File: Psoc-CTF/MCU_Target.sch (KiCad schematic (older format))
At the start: 69 parts, among them IC1 CY8C4248LQI-BL583, J4 Conn_01x04, J5 USB3076-XX-X_REVC, J6 Header 9x2, J7 Header 9x2, P1 Power, P2 Analog, P3 Digital, P4 Digital, P5 CONN_01X01, P6 CONN_01X01, P7 CONN_01X01, P8 CONN_01X01, U4 FM24C04B-GTR, U5 CY7C65211-24LTXI, Y1 24MHz, Y2 32.768Khz

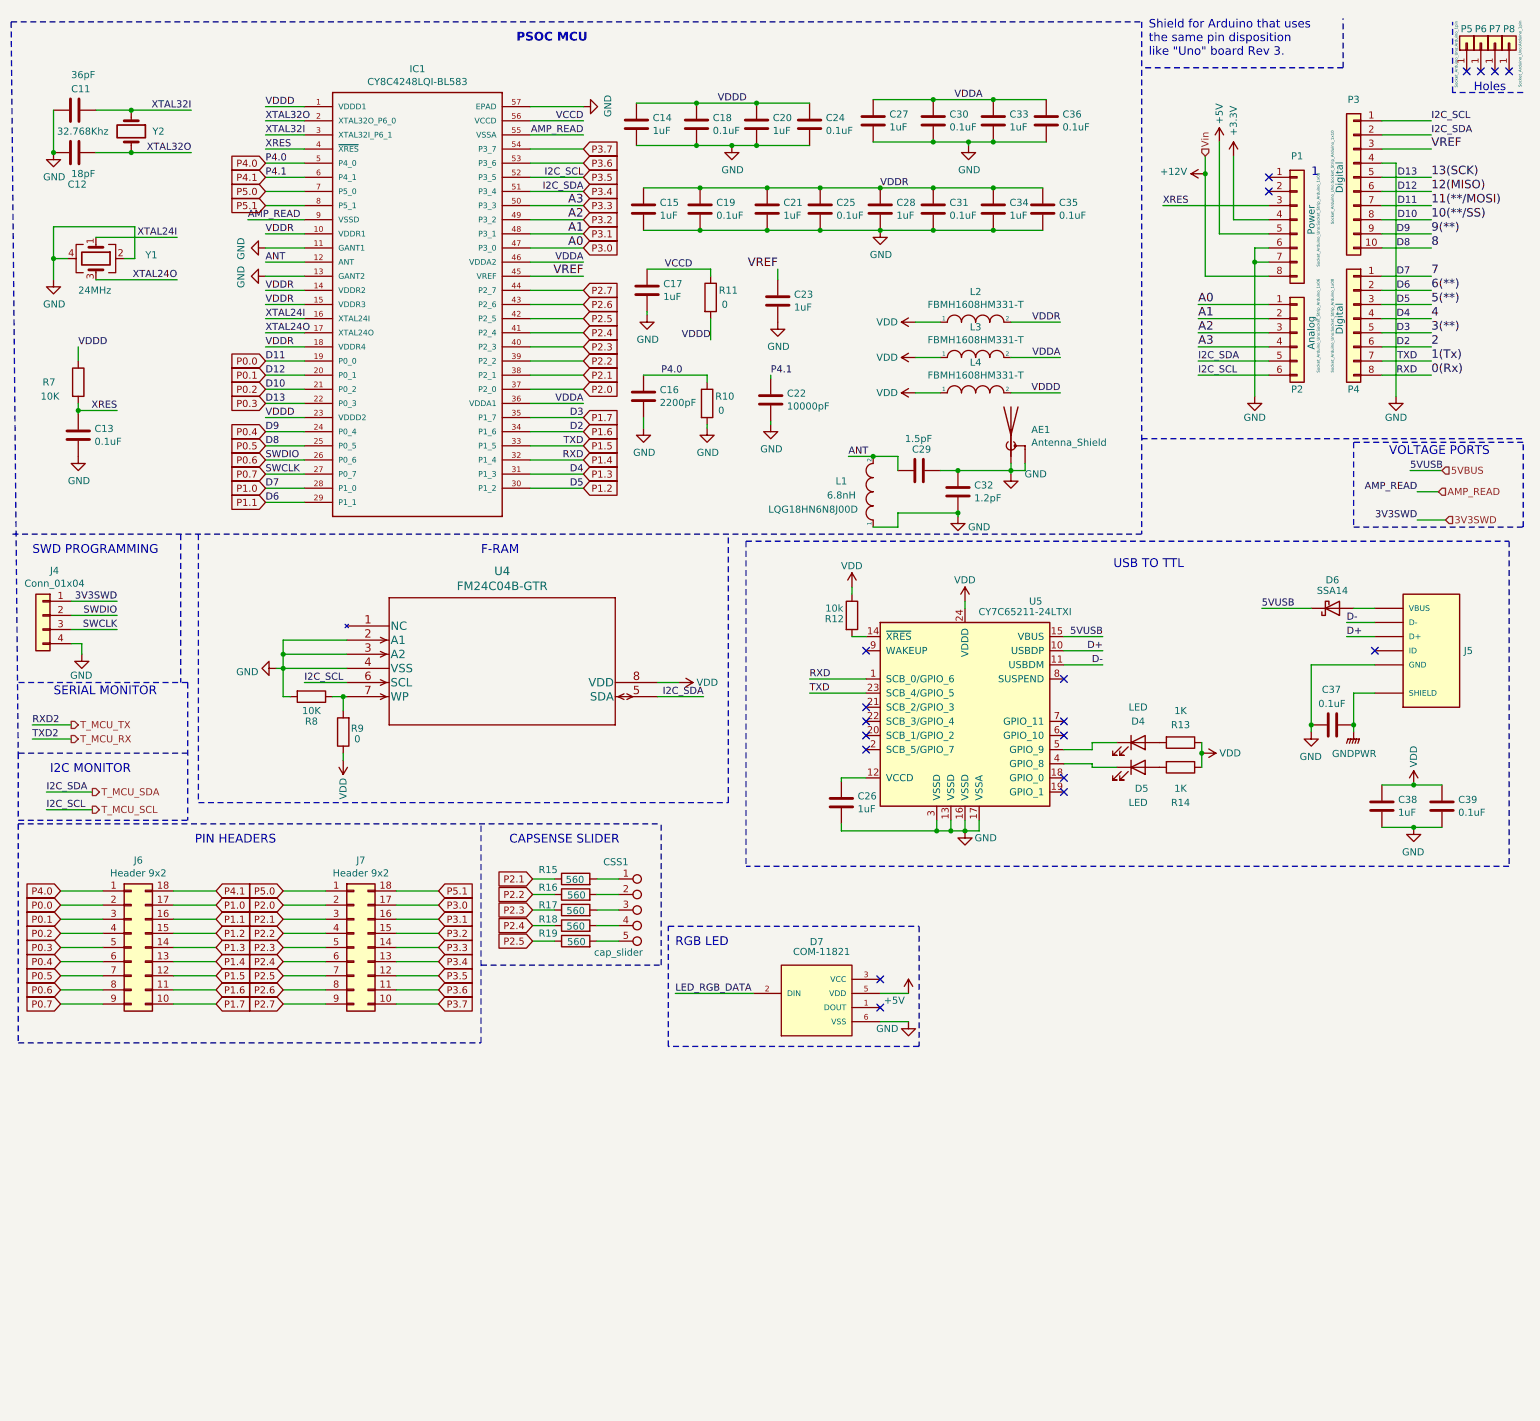
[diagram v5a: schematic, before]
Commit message: Anexo de nuevos pulsadores y arreglo de resistencias
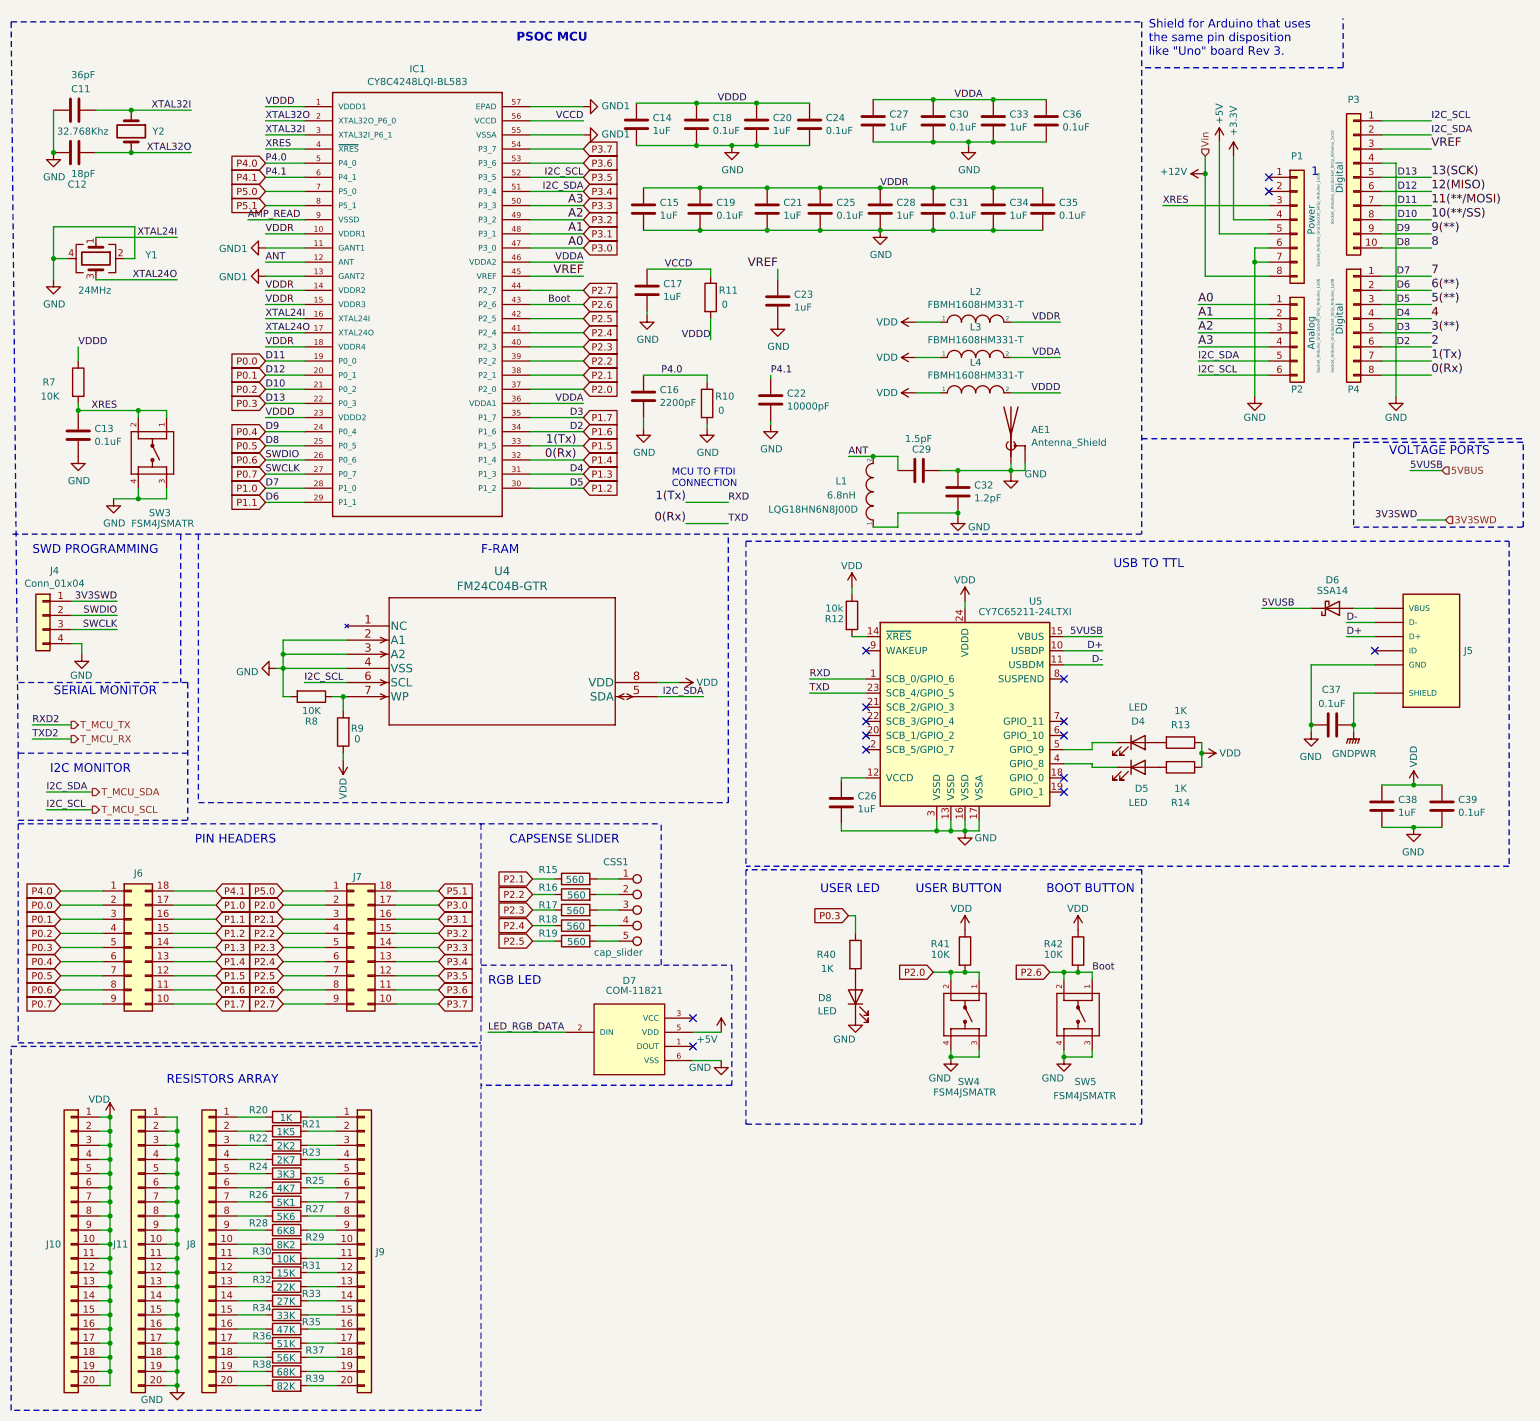
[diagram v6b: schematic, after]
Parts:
- removed P5, P6, P7, P8: CONN_01X01, Socket_Arduino_Uno:Arduino_1pin, symbol Connector_Generic:Conn_01x01
- added D8: LED, LED_SMD:LED_0603_1608Metric_Pad1.05x0.95mm_HandSolder, symbol Device:LED
- added J10, J11, J8, J9: Conn_01x20, Connector_PinHeader_2.54mm:PinHeader_1x20_P2.54mm_Vertical, symbol Connector_Generic:Conn_01x20
- added R20, R40: 1K, Resistor_SMD:R_0603_1608Metric_Pad0.98x0.95mm_HandSolder, symbol Device:R
- added R21: 1K5, Resistor_SMD:R_0603_1608Metric_Pad0.98x0.95mm_HandSolder, symbol Device:R
- added R22: 2K2, Resistor_SMD:R_0603_1608Metric_Pad0.98x0.95mm_HandSolder, symbol Device:R
- added R23: 2K7, Resistor_SMD:R_0603_1608Metric_Pad0.98x0.95mm_HandSolder, symbol Device:R
- added R24: 3K3, Resistor_SMD:R_0603_1608Metric_Pad0.98x0.95mm_HandSolder, symbol Device:R
- added R25: 4K7, Resistor_SMD:R_0603_1608Metric_Pad0.98x0.95mm_HandSolder, symbol Device:R
- added R26: 5K1, Resistor_SMD:R_0603_1608Metric_Pad0.98x0.95mm_HandSolder, symbol Device:R
- added R27: 5K6, Resistor_SMD:R_0603_1608Metric_Pad0.98x0.95mm_HandSolder, symbol Device:R
- added R28: 6K8, Resistor_SMD:R_0603_1608Metric_Pad0.98x0.95mm_HandSolder, symbol Device:R
- added R29: 8K2, Resistor_SMD:R_0603_1608Metric_Pad0.98x0.95mm_HandSolder, symbol Device:R
- added R30, R41, R42: 10K, Resistor_SMD:R_0603_1608Metric_Pad0.98x0.95mm_HandSolder, symbol Device:R
- added R31: 15K, Resistor_SMD:R_0603_1608Metric_Pad0.98x0.95mm_HandSolder, symbol Device:R
- added R32: 22K, Resistor_SMD:R_0603_1608Metric_Pad0.98x0.95mm_HandSolder, symbol Device:R
- added R33: 27K, Resistor_SMD:R_0603_1608Metric_Pad0.98x0.95mm_HandSolder, symbol Device:R
- added R34: 33K, Resistor_SMD:R_0603_1608Metric_Pad0.98x0.95mm_HandSolder, symbol Device:R
- added R35: 47K, Resistor_SMD:R_0603_1608Metric_Pad0.98x0.95mm_HandSolder, symbol Device:R
- added R36: 51K, Resistor_SMD:R_0603_1608Metric_Pad0.98x0.95mm_HandSolder, symbol Device:R
- added R37: 56K, Resistor_SMD:R_0603_1608Metric_Pad0.98x0.95mm_HandSolder, symbol Device:R
- added R38: 68K, Resistor_SMD:R_0603_1608Metric_Pad0.98x0.95mm_HandSolder, symbol Device:R
- added R39: 82K, Resistor_SMD:R_0603_1608Metric_Pad0.98x0.95mm_HandSolder, symbol Device:R
- added SW3, SW4, SW5: FSM4JSMATR, Psoc-CTF:Push_button_FSM4JSMATR, symbol Push_button_FSM4JSMATR:4-1437565-2
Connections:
- net AMP_READ: no longer IC1.55 (VSSA)
- net GND: now also D8.1 (K), J11.1 (Pin_1), J11.10 (Pin_10), J11.11 (Pin_11), J11.12 (Pin_12), J11.13 (Pin_13), J11.14 (Pin_14), J11.15 (Pin_15), J11.16 (Pin_16), J11.17 (Pin_17), J11.18 (Pin_18), J11.19 (Pin_19), J11.2 (Pin_2), J11.20 (Pin_20), J11.3 (Pin_3), J11.4 (Pin_4), J11.5 (Pin_5), J11.6 (Pin_6), J11.7 (Pin_7), J11.8 (Pin_8), J11.9 (Pin_9), SW3.3, SW3.4, SW4.3, SW4.4, SW5.3, SW5.4; no longer IC1.11 (GANT1), IC1.13 (GANT2), IC1.57 (EPAD)
- net P0.3: now also R40.1
- net P1.4: now also U5.23 (SCB_4/GPIO_5); no longer U5.1 (SCB_0/GPIO_6)
- net P1.5: now also U5.1 (SCB_0/GPIO_6); no longer U5.23 (SCB_4/GPIO_5)
- net P2.0: now also R41.2, SW4.1, SW4.2
- net P2.6: now also R42.2, SW5.1, SW5.2
- net VDD: now also J10.1 (Pin_1), J10.10 (Pin_10), J10.11 (Pin_11), J10.12 (Pin_12), J10.13 (Pin_13), J10.14 (Pin_14), J10.15 (Pin_15), J10.16 (Pin_16), J10.17 (Pin_17), J10.18 (Pin_18), J10.19 (Pin_19), J10.2 (Pin_2), J10.20 (Pin_20), J10.3 (Pin_3), J10.4 (Pin_4), J10.5 (Pin_5), J10.6 (Pin_6), J10.7 (Pin_7), J10.8 (Pin_8), J10.9 (Pin_9), R41.1, R42.1
- net XRES: now also SW3.1, SW3.2
- new net: J8.1 (Pin_1), R20.1
- new net: J9.1 (Pin_1), R20.2
- new net: J8.2 (Pin_2), R21.1
- new net: J9.2 (Pin_2), R21.2
- new net: J8.3 (Pin_3), R22.1
- new net: J9.3 (Pin_3), R22.2
- new net: J8.4 (Pin_4), R23.1
- new net: J9.4 (Pin_4), R23.2
- new net: J8.5 (Pin_5), R24.1
- new net: J9.5 (Pin_5), R24.2
- new net: J8.6 (Pin_6), R25.1
- new net: J9.6 (Pin_6), R25.2
- new net: J8.8 (Pin_8), R27.1
- new net: J9.8 (Pin_8), R27.2
- new net: J8.9 (Pin_9), R28.1
- new net: J9.9 (Pin_9), R28.2
- new net: J8.10 (Pin_10), R29.1
- new net: J9.10 (Pin_10), R29.2
- new net: J8.7 (Pin_7), R26.1
- new net: J9.7 (Pin_7), R26.2
- new net: J8.11 (Pin_11), R30.1
- new net: J9.11 (Pin_11), R30.2
- new net: J8.12 (Pin_12), R31.1
- new net: J9.12 (Pin_12), R31.2
- new net: J8.13 (Pin_13), R32.1
- new net: J9.13 (Pin_13), R32.2
- new net: J8.14 (Pin_14), R33.1
- new net: J9.14 (Pin_14), R33.2
- new net: J8.15 (Pin_15), R34.1
- new net: J9.15 (Pin_15), R34.2
- new net: J8.16 (Pin_16), R35.1
- new net: J9.16 (Pin_16), R35.2
- new net: J8.18 (Pin_18), R37.1
- new net: J9.18 (Pin_18), R37.2
- new net: J8.19 (Pin_19), R38.1
- new net: J9.19 (Pin_19), R38.2
- new net: J8.20 (Pin_20), R39.1
- new net: J9.20 (Pin_20), R39.2
- new net: J8.17 (Pin_17), R36.1
- new net: J9.17 (Pin_17), R36.2
- new net: D8.2 (A), R40.2
- new net GND1: IC1.11 (GANT1), IC1.13 (GANT2), IC1.55 (VSSA), IC1.57 (EPAD)
- no-connect marks 19 -> 15
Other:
- note added: "BOOT BUTTON"
- note added: "MCU TO FTDI\nCONNECTION"
- note added: "RESISTORS ARRAY"
- note added: "USER BUTTON"
- note added: "USER LED"
- note removed: "Holes"
- moved on the sheet: D7

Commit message: Ruteo Psoc-CTF
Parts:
- removed J6, J7: Header 9x2, Connector_PinHeader_2.54mm:PinHeader_2x09_P2.54mm_Vertical, symbol Connector_Generic:Conn_02x09_Counter_Clockwise
- added J6: Conn_01x10, Connector_PinHeader_2.54mm:PinHeader_1x10_P2.54mm_Vertical, symbol Connector_Generic:Conn_01x10
- added J7: Conn_01x04, Connector_PinHeader_2.54mm:PinHeader_1x04_P2.54mm_Vertical, symbol Connector_Generic:Conn_01x04
- AE1: footprint Psoc-CTF:Antena_pad -> Psoc-CTF:Antenna_pad
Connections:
- net AMP_READ is gone; now on net GND1: IC1.9 (VSSD)
- net GND: now also J10.1 (Pin_1), J10.10 (Pin_10), J10.11 (Pin_11), J10.12 (Pin_12), J10.13 (Pin_13), J10.14 (Pin_14), J10.15 (Pin_15), J10.16 (Pin_16), J10.17 (Pin_17), J10.18 (Pin_18), J10.19 (Pin_19), J10.2 (Pin_2), J10.20 (Pin_20), J10.3 (Pin_3), J10.4 (Pin_4), J10.5 (Pin_5), J10.6 (Pin_6), J10.7 (Pin_7), J10.8 (Pin_8), J10.9 (Pin_9), J6.10 (Pin_10); no longer J11.1 (Pin_1), J11.10 (Pin_10), J11.11 (Pin_11), J11.12 (Pin_12), J11.13 (Pin_13), J11.14 (Pin_14), J11.15 (Pin_15), J11.16 (Pin_16), J11.17 (Pin_17), J11.18 (Pin_18), J11.19 (Pin_19), J11.2 (Pin_2), J11.20 (Pin_20), J11.3 (Pin_3), J11.4 (Pin_4), J11.5 (Pin_5), J11.6 (Pin_6), J11.7 (Pin_7), J11.8 (Pin_8), J11.9 (Pin_9)
- net P1.0: now also R41.2, SW4.1, SW4.2
- net P1.1: now also R42.2, SW5.1, SW5.2
- net P2.0: now also P2.1 (Pin_1); no longer R41.2, SW4.1, SW4.2
- net P2.1: now also P2.2 (Pin_2)
- net P2.2: now also P2.3 (Pin_3)
- net P2.3: now also P2.4 (Pin_4)
- net P2.4: now also P2.5 (Pin_5)
- net P2.5: now also P2.6 (Pin_6)
- net P2.6: now also J6.2 (Pin_2); no longer R42.2, SW5.1, SW5.2
- net P2.7: now also J6.3 (Pin_3)
- net P3.0: now also J6.4 (Pin_4); no longer P2.1 (Pin_1)
- net P3.1: now also J6.5 (Pin_5); no longer P2.2 (Pin_2)
- net P3.2: now also J6.6 (Pin_6); no longer P2.3 (Pin_3)
- net P3.3: now also J6.7 (Pin_7); no longer P2.4 (Pin_4)
- net P3.4: no longer P2.5 (Pin_5)
- net P3.5: no longer P2.6 (Pin_6)
- net P3.6: now also J6.8 (Pin_8)
- net P3.7: now also J6.9 (Pin_9)
- net P4.0: now also J7.4 (Pin_4)
- net P4.1: now also J7.3 (Pin_3)
- net P5.0: now also J7.2 (Pin_2)
- net P5.1: now also J7.1 (Pin_1)
- net VDD: now also J11.1 (Pin_1), J11.10 (Pin_10), J11.11 (Pin_11), J11.12 (Pin_12), J11.13 (Pin_13), J11.14 (Pin_14), J11.15 (Pin_15), J11.16 (Pin_16), J11.17 (Pin_17), J11.18 (Pin_18), J11.19 (Pin_19), J11.2 (Pin_2), J11.20 (Pin_20), J11.3 (Pin_3), J11.4 (Pin_4), J11.5 (Pin_5), J11.6 (Pin_6), J11.7 (Pin_7), J11.8 (Pin_8), J11.9 (Pin_9), J6.1 (Pin_1); no longer J10.1 (Pin_1), J10.10 (Pin_10), J10.11 (Pin_11), J10.12 (Pin_12), J10.13 (Pin_13), J10.14 (Pin_14), J10.15 (Pin_15), J10.16 (Pin_16), J10.17 (Pin_17), J10.18 (Pin_18), J10.19 (Pin_19), J10.2 (Pin_2), J10.20 (Pin_20), J10.3 (Pin_3), J10.4 (Pin_4), J10.5 (Pin_5), J10.6 (Pin_6), J10.7 (Pin_7), J10.8 (Pin_8), J10.9 (Pin_9)
- net 5VBUS renamed VBUS

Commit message: Corrrecciones y anexo de logo
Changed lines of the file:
@@
 	1    0    0    -1
 $EndComp
-Connection ~ 1675 10175
 $Comp
 L Push_button_FSM4JSMATR:4-1437565-2 SW?
@@
 P 1675 8275
 AR Path="/62ABADE4" Ref="#PWR?"  Part="1"
-AR Path="/62149449/62ABADE4" Ref="#PWR?"  Part="1"
-F 0 "#PWR?" H 1675 8125 50  0001 C CNN
+AR Path="/62149449/62ABADE4" Ref="#PWR063"  Part="1"
+F 0 "#PWR063" H 1675 8125 50  0001 C CNN
 F 1 "VDD" H 1675 8400 50  0000 L CNN
 F 2 "" H 1675 8275 50  0001 C CNN
